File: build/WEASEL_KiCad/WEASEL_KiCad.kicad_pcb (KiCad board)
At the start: 2 copper layers, 355 x 80 mm, 56 parts

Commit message: Layout design
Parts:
- added REF**: Panel Jack, SimpleSynthPanel:Panel Jack, F.Cu at (314.0, 60.0)
- added REF**: Panel Jack, SimpleSynthPanel:Panel Jack, F.Cu at (244.0, 90.0)
- added REF**: Panel Jack, SimpleSynthPanel:Panel Jack, F.Cu at (269.0, 127.5)
- added REF**: Panel Jack, SimpleSynthPanel:Panel Jack, F.Cu at (244.0, 135.0)
- added REF**: Panel Jack, SimpleSynthPanel:Panel Jack, F.Cu at (304.0, 67.5)
- added REF**: Panel Jack, SimpleSynthPanel:Panel Jack, F.Cu at (314.0, 75.0)
- added REF**: Panel Jack, SimpleSynthPanel:Panel Jack, F.Cu at (279.0, 90.0)
- added REF**: Panel Jack, SimpleSynthPanel:Panel Jack, F.Cu at (244.0, 120.0)
- added REF**: Panel Jack, SimpleSynthPanel:Panel Jack, F.Cu at (259.0, 135.0)
- added REF**: Panel Jack, SimpleSynthPanel:Panel Jack, F.Cu at (304.0, 97.5)
- added REF**: Panel Jack, SimpleSynthPanel:Panel Jack, F.Cu at (314.0, 120.0)
- added REF**: Panel Jack, SimpleSynthPanel:Panel Jack, F.Cu at (259.0, 120.0)
- added REF**: Panel Jack, SimpleSynthPanel:Panel Jack, F.Cu at (314.0, 105.0)
- added REF**: Panel Jack, SimpleSynthPanel:Panel Jack, F.Cu at (244.0, 105.0)
- added REF**: Panel Jack, SimpleSynthPanel:Panel Jack, F.Cu at (224.0, 135.0)
- added REF**: Panel Jack, SimpleSynthPanel:Panel Jack, F.Cu at (294.0, 135.0)
- added REF**: Panel Jack, SimpleSynthPanel:Panel Jack, F.Cu at (304.0, 127.5)
- added REF**: Panel Jack, SimpleSynthPanel:Panel Jack, F.Cu at (279.0, 105.0)
- added REF**: Panel Jack, SimpleSynthPanel:Panel Jack, F.Cu at (314.0, 135.0)
- added REF**: ToggleSwitch_MTS-202_DPDT, DIYSynthMNL:PanelHole_ToggleSwitch_MTS-202, F.Cu at (105.0, 124.5)
- added REF**: Panel Jack, SimpleSynthPanel:Panel Jack, F.Cu at (193.5, 127.5)
- added REF**: Panel Jack, SimpleSynthPanel:Panel Jack, F.Cu at (294.0, 105.0)
- added REF**: Panel Jack, SimpleSynthPanel:Panel Jack, F.Cu at (259.0, 105.0)
- added REF**: Panel Jack, SimpleSynthPanel:Panel Jack, F.Cu at (224.0, 120.0)
- added REF**: Panel Jack, SimpleSynthPanel:Panel Jack, F.Cu at (259.0, 75.0)
- added REF**: Panel Jack, SimpleSynthPanel:Panel Jack, F.Cu at (279.0, 60.0)
- added REF**: Panel Jack, SimpleSynthPanel:Panel Jack, F.Cu at (224.0, 90.0)
- added REF**: Panel Jack, SimpleSynthPanel:Panel Jack, F.Cu at (224.0, 105.0)
- added REF**: Panel Jack, SimpleSynthPanel:Panel Jack, F.Cu at (234.0, 127.5)
- added REF**: Panel Jack, SimpleSynthPanel:Panel Jack, F.Cu at (259.0, 90.0)
- added REF**: Panel Jack, SimpleSynthPanel:Panel Jack, F.Cu at (279.0, 75.0)
- added REF**: ToggleSwitch_MTS-202_DPDT, DIYSynthMNL:PanelHole_ToggleSwitch_MTS-202, F.Cu at (198.5, 103.5)
- added REF**: Panel Jack, SimpleSynthPanel:Panel Jack, F.Cu at (279.0, 120.0)
- added REF**: Panel Jack, SimpleSynthPanel:Panel Jack, F.Cu at (294.0, 75.0)
- added REF**: Panel Jack, SimpleSynthPanel:Panel Jack, F.Cu at (234.0, 97.5)
- added REF**: Panel Jack, SimpleSynthPanel:Panel Jack, F.Cu at (203.5, 120.0)
- added REF**: Panel Jack, SimpleSynthPanel:Panel Jack, F.Cu at (203.5, 135.0)
- added REF**: Panel Jack, SimpleSynthPanel:Panel Jack, F.Cu at (314.0, 90.0)
- added REF**: Panel Jack, SimpleSynthPanel:Panel Jack, F.Cu at (269.0, 67.5)
- added REF**: Panel Jack, SimpleSynthPanel:Panel Jack, F.Cu at (269.0, 97.5)
- added REF**: ToggleSwitch_MTS-202_DPDT, DIYSynthMNL:PanelHole_ToggleSwitch_MTS-202, F.Cu at (105.0, 109.5)
- added REF**: Panel Jack, SimpleSynthPanel:Panel Jack, F.Cu at (279.0, 135.0)
- added REF**: Panel Jack, SimpleSynthPanel:Panel Jack, F.Cu at (259.0, 60.0)
- moved ? 377.0 mm to (-12.0, 90.0)
- moved ? 377.0 mm to (-12.0, 160.0)
- moved REF** 208.8 mm to (224.0, 75.0)
- moved REF** 208.8 mm to (224.0, 60.0)
- moved REF** 204.9 mm to (234.0, 67.5)
- moved REF** 201.1 mm to (244.0, 60.0)
- moved REF** 201.1 mm to (244.0, 75.0)
- moved REF** 165.2 mm to (117.5, 65.0)
- moved REF** 159.1 mm to (204.0, 80.0) (x2)
- moved REF** 159.1 mm to (166.5, 65.0)
- moved REF** 159.1 mm to (189.0, 80.0) (x2)
- moved REF** 159.1 mm to (159.0, 80.0)
- moved REF** 159.1 mm to (174.0, 80.0)
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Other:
- board size 355 x 80 mm -> 313 x 99 mm
- board text added: "- +"
- board text added: "Attack"
- board text added: "COMPLEX OSCILLATOR"
- board text added: "Complex Osc. Pitch"
- board text added: "Complex Osc. Timbre"
- board text added: "ENVELOPE"
- board text added: "Envelope Generator"
- board text added: "Fine Tune"
- board text added: "Frequency"
- board text added: "LOW-PASS GATE/VCA"
- board text added: "Level 1"
- board text added: "Level 2"
- board text added: "MODULATION OSCILLATOR"
- board text added: "Mod Osc. Frequency"
- board text added: "Mod Osc. Modulation"
- board text added: "Modulation"
- board text added: "PULSER"
- board text added: "PWM"
- board text added: "Pitch"
- board text added: "Pulser"
- board text added: "RANDOM VOLTAGE"
- board text added: "Random Voltage"
- board text added: "Release"
- board text added: "SEQUENCER"
- board text added: "Sequencer"
- board text added: "Sustain"
- board text added: "Timbre"

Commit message: Virtual Patch bay added to schematic
Virtual modular patch bay added
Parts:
- moved REF** 374.4 mm to (-60.0, 77.0)
- moved REF** 374.4 mm to (-130.0, 107.0)
- moved REF** 374.4 mm to (-105.0, 144.5)
- moved REF** 374.4 mm to (-130.0, 152.0)
- moved REF** 374.4 mm to (-70.0, 84.5)
- moved REF** 374.4 mm to (-170.0, 97.0)
- moved REF** 374.4 mm to (-150.0, 92.0)
- moved REF** 374.4 mm to (-299.0, 134.0)
- moved REF** 374.4 mm to (-329.0, 119.0)
- moved REF** 374.4 mm to (-130.0, 77.0)
- moved REF** 374.4 mm to (-60.0, 92.0)
- moved REF** 374.4 mm to (-329.0, 149.0)
- moved REF** 374.4 mm to (-279.0, 82.0)
- moved REF** 374.4 mm to (-329.0, 134.0)
- moved REF** 374.4 mm to (-256.5, 82.0)
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
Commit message: Schematic and PCB Changes
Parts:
- removed ? (x3): , 
- removed REF** (x45): Panel Jack, SimpleSynthPanel:Panel Jack
- removed REF** (x27): Panel Knob 1P, SimpleSynthPanel:Panel Knob 1P
- removed REF** (x15): ToggleSwitch_MTS-202_DPDT, DIYSynthMNL:PanelHole_ToggleSwitch_MTS-202
- removed REF** (x7): LED_HOLE, DIYSynthMNL:LED_HOLE
- removed REF**: MountingHole_M3_Standoff, DIYSynthMNL:MountingHole_M3_Standoff
- added C1: 10nF, DIYSynthMNL:C_Rect_L7.0mm_W2.0mm_P5.00mm_BigPads, F.Cu at (-3.00, 100.5)
- added C10: 10nF, DIYSynthMNL:C_Rect_L7.0mm_W2.0mm_P5.00mm_BigPads, F.Cu at (5.55, 100.5)
- added C11: 10nF, DIYSynthMNL:C_Rect_L7.0mm_W2.0mm_P5.00mm_BigPads, F.Cu at (5.55, 104.0)
- added C12: 10nF, DIYSynthMNL:C_Rect_L7.0mm_W2.0mm_P5.00mm_BigPads, F.Cu at (5.55, 107.6)
- added C13: 10nF, DIYSynthMNL:C_Rect_L7.0mm_W2.0mm_P5.00mm_BigPads, F.Cu at (5.55, 111.2)
- added C14: 10nF, DIYSynthMNL:C_Rect_L7.0mm_W2.0mm_P5.00mm_BigPads, F.Cu at (5.55, 114.7)
- added C15: 10nF, DIYSynthMNL:C_Rect_L7.0mm_W2.0mm_P5.00mm_BigPads, F.Cu at (5.55, 118.2)
- added C16: 10nF, DIYSynthMNL:C_Rect_L7.0mm_W2.0mm_P5.00mm_BigPads, F.Cu at (5.55, 121.8)
- added C17: 10nF, DIYSynthMNL:C_Rect_L7.0mm_W2.0mm_P5.00mm_BigPads, F.Cu at (-250.6, 162.7)
- added C18: 10nF, DIYSynthMNL:C_Rect_L7.0mm_W2.0mm_P5.00mm_BigPads, F.Cu at (-250.6, 166.2)
- added C19: 10nF, DIYSynthMNL:C_Rect_L7.0mm_W2.0mm_P5.00mm_BigPads, F.Cu at (-242.0, 137.8)
- added C2: 10nF, DIYSynthMNL:C_Rect_L7.0mm_W2.0mm_P5.00mm_BigPads, F.Cu at (-3.00, 104.0)
- added C20: 10nF, DIYSynthMNL:C_Rect_L7.0mm_W2.0mm_P5.00mm_BigPads, F.Cu at (-242.0, 141.4)
- added C21: 10nF, DIYSynthMNL:C_Rect_L7.0mm_W2.0mm_P5.00mm_BigPads, F.Cu at (-242.0, 144.9)
- added C22: 10nF, DIYSynthMNL:C_Rect_L7.0mm_W2.0mm_P5.00mm_BigPads, F.Cu at (-242.0, 148.5)
- added C23: 10nF, DIYSynthMNL:C_Rect_L7.0mm_W2.0mm_P5.00mm_BigPads, F.Cu at (-242.0, 152.0)
- added C24: 10nF, DIYSynthMNL:C_Rect_L7.0mm_W2.0mm_P5.00mm_BigPads, F.Cu at (-242.0, 155.6)
- added C25: 10nF, DIYSynthMNL:C_Rect_L7.0mm_W2.0mm_P5.00mm_BigPads, F.Cu at (-242.0, 159.1)
- added C26: 10nF, DIYSynthMNL:C_Rect_L7.0mm_W2.0mm_P5.00mm_BigPads, F.Cu at (-242.0, 162.7)
- added C3: 10nF, DIYSynthMNL:C_Rect_L7.0mm_W2.0mm_P5.00mm_BigPads, F.Cu at (-3.00, 107.6)
- added C4: 10nF, DIYSynthMNL:C_Rect_L7.0mm_W2.0mm_P5.00mm_BigPads, F.Cu at (-3.00, 111.2)
- added C5: 10nF, DIYSynthMNL:C_Rect_L7.0mm_W2.0mm_P5.00mm_BigPads, F.Cu at (-3.00, 114.7)
- added C6: 10nF, DIYSynthMNL:C_Rect_L7.0mm_W2.0mm_P5.00mm_BigPads, F.Cu at (-3.00, 118.2)
- added C7: 10nF, DIYSynthMNL:C_Rect_L7.0mm_W2.0mm_P5.00mm_BigPads, F.Cu at (-3.00, 121.8)
- added C8: 10nF, DIYSynthMNL:C_Rect_L7.0mm_W2.0mm_P5.00mm_BigPads, F.Cu at (-3.00, 125.3)
- added C9: 10nF, DIYSynthMNL:C_Rect_L7.0mm_W2.0mm_P5.00mm_BigPads, F.Cu at (-3.00, 128.9)
- added D1: 1N4148, DIYSynthMNL:D_4148_BigPads, F.Cu at (-259.0, 76.8)
- added D2: 1N4148, DIYSynthMNL:D_4148_BigPads, F.Cu at (-259.0, 80.4)
- added D3: 1N4148, DIYSynthMNL:D_4148_BigPads, F.Cu at (-259.0, 83.9)
- added D30: 1N4148, DIYSynthMNL:D_4148_BigPads, F.Cu at (-247.5, 76.8)
- added D31: 1N4148, DIYSynthMNL:D_4148_BigPads, F.Cu at (-247.5, 80.4)
- added D32: 1N4148, DIYSynthMNL:D_4148_BigPads, F.Cu at (-247.5, 83.9)
- added D33: 1N4148, DIYSynthMNL:D_4148_BigPads, F.Cu at (-247.5, 87.5)
- added D34: 1N4148, DIYSynthMNL:D_4148_BigPads, F.Cu at (-247.5, 91.0)
- added D35: 1N4148, DIYSynthMNL:D_4148_BigPads, F.Cu at (-247.5, 94.6)
- added D36: 1N4148, DIYSynthMNL:D_4148_BigPads, F.Cu at (-247.5, 98.1)
- added D37: 1N4148, DIYSynthMNL:D_4148_BigPads, F.Cu at (-247.5, 101.7)
- added D38: 1N4148, DIYSynthMNL:D_4148_BigPads, F.Cu at (-236.1, 76.8)
- added D39: 1N4148, DIYSynthMNL:D_4148_BigPads, F.Cu at (-236.1, 80.4)
- added D4: 1N4148, DIYSynthMNL:D_4148_BigPads, F.Cu at (-259.0, 87.5)
- added D40: 1N4148, DIYSynthMNL:D_4148_BigPads, F.Cu at (-236.1, 83.9)
- added D41: 1N4148, DIYSynthMNL:D_4148_BigPads, F.Cu at (-236.1, 87.5)
- added D42: 1N4148, DIYSynthMNL:D_4148_BigPads, F.Cu at (-236.1, 91.0)
- added D43: 1N4148, DIYSynthMNL:D_4148_BigPads, F.Cu at (-236.1, 94.6)
- added D44: 1N4148, DIYSynthMNL:D_4148_BigPads, F.Cu at (297.6, 43.5)
- added D45: 1N4148, DIYSynthMNL:D_4148_BigPads, F.Cu at (-213.0, 109.3)
- added D46: 1N4148, DIYSynthMNL:D_4148_BigPads, F.Cu at (-213.0, 112.8)
- added D47: 1N4148, DIYSynthMNL:D_4148_BigPads, F.Cu at (-213.0, 116.4)
- added D48: 1N4148, DIYSynthMNL:D_4148_BigPads, F.Cu at (-213.0, 120.0)
- added D49: 1N4148, DIYSynthMNL:D_4148_BigPads, F.Cu at (-213.0, 123.5)
- added D5: 1N4148, DIYSynthMNL:D_4148_BigPads, F.Cu at (-259.0, 91.0)
- added D6: 1N4148, DIYSynthMNL:D_4148_BigPads, F.Cu at (-259.0, 94.6)
- added D7: 1N4148, DIYSynthMNL:D_4148_BigPads, F.Cu at (-259.0, 98.1)
- added D8: 1N4148, DIYSynthMNL:D_4148_BigPads, F.Cu at (-259.0, 101.7)
- added J1: MIDI IN, Connector_Audio:Jack_3.5mm_CUI_SJ1-3523N_Horizontal, F.Cu at (294.3, 30.0)
- added J10: LPG_LEVEL2CTRL, Connector_Audio:Jack_3.5mm_QingPu_WQP-PJ398SM_Vertical_CircularHoles, F.Cu at (215.0, 161.7)
- added J14: SEQ_OUTPUT2, Connector_Audio:Jack_3.5mm_QingPu_WQP-PJ398SM_Vertical_CircularHoles, F.Cu at (125.0, 151.7)
- added J15: SEQ_OUTPUT3, Connector_Audio:Jack_3.5mm_QingPu_WQP-PJ398SM_Vertical_CircularHoles, F.Cu at (185.0, 151.7)
- added J16: EG_OUTPUT1, Connector_Audio:Jack_3.5mm_QingPu_WQP-PJ398SM_Vertical_CircularHoles, F.Cu at (110.0, 151.7)
- added J17: EG_OUTPUT2, Connector_Audio:Jack_3.5mm_QingPu_WQP-PJ398SM_Vertical_CircularHoles, F.Cu at (170.0, 151.7)
- added J18: EG_OUTPUT3, Connector_Audio:Jack_3.5mm_QingPu_WQP-PJ398SM_Vertical_CircularHoles, F.Cu at (230.0, 151.7)
- added J19: PLSR_OUTPUT1, Connector_Audio:Jack_3.5mm_QingPu_WQP-PJ398SM_Vertical_CircularHoles, F.Cu at (50.0, 171.7)
- added J2: STEREO_OUTPUT, Connector_Audio:Jack_3.5mm_CUI_SJ1-3523N_Horizontal, F.Cu at (275.5, 30.0)
- added J20: PLSR_OUTPUT2, Connector_Audio:Jack_3.5mm_QingPu_WQP-PJ398SM_Vertical_CircularHoles, F.Cu at (125.0, 171.7)
- added J21: PLSR_OUTPUT3, Connector_Audio:Jack_3.5mm_QingPu_WQP-PJ398SM_Vertical_CircularHoles, F.Cu at (185.0, 171.7)
- added J22: RNDM_OUTPUT1, Connector_Audio:Jack_3.5mm_QingPu_WQP-PJ398SM_Vertical_CircularHoles, F.Cu at (110.0, 171.7)
- added J23: RNDM_OUTPUT2, Connector_Audio:Jack_3.5mm_QingPu_WQP-PJ398SM_Vertical_CircularHoles, F.Cu at (170.0, 171.7)
- added J24: RNDM_OUTPUT3, Connector_Audio:Jack_3.5mm_QingPu_WQP-PJ398SM_Vertical_CircularHoles, F.Cu at (230.0, 171.7)
- added J3: SEQ_OUTPUT1, Connector_Audio:Jack_3.5mm_QingPu_WQP-PJ398SM_Vertical_CircularHoles, F.Cu at (50.0, 151.7)
- added J4: PLSR_PERIODCTRL, Connector_Audio:Jack_3.5mm_QingPu_WQP-PJ398SM_Vertical_CircularHoles, F.Cu at (65.0, 161.7)
- added J5: MODOSC_FREQCTRL, Connector_Audio:Jack_3.5mm_QingPu_WQP-PJ398SM_Vertical_CircularHoles, F.Cu at (80.0, 161.7)
- added J6: MODOSC_MODCTRL, Connector_Audio:Jack_3.5mm_QingPu_WQP-PJ398SM_Vertical_CircularHoles, F.Cu at (95.0, 161.7)
- added J7: COMPOSC_PITCHCTRL, Connector_Audio:Jack_3.5mm_QingPu_WQP-PJ398SM_Vertical_CircularHoles, F.Cu at (140.0, 161.7)
- added J8: COMPOSC_WAVEFOLDERCTRL, Connector_Audio:Jack_3.5mm_QingPu_WQP-PJ398SM_Vertical_CircularHoles, F.Cu at (155.0, 161.7)
- added J9: LPG_LEVEL1CTRL, Connector_Audio:Jack_3.5mm_QingPu_WQP-PJ398SM_Vertical_CircularHoles, F.Cu at (200.0, 161.7)
- added R1: 10k, PCM_4ms_Resistor:R_Axial_DIN0207_L6.3mm_D2.5mm_P7.62mm_Horizontal, F.Cu at (307.0, 57.0)
- added R10: 220R, PCM_4ms_Resistor:R_Axial_DIN0207_L6.3mm_D2.5mm_P7.62mm_Horizontal, F.Cu at (295.4, 39.5)
- added R2: 10k, PCM_4ms_Resistor:R_Axial_DIN0207_L6.3mm_D2.5mm_P7.62mm_Horizontal, F.Cu at (307.0, 59.5)
- added R3: 10k, PCM_4ms_Resistor:R_Axial_DIN0207_L6.3mm_D2.5mm_P7.62mm_Horizontal, F.Cu at (336.3, 67.0)
- added R4: 10k, PCM_4ms_Resistor:R_Axial_DIN0207_L6.3mm_D2.5mm_P7.62mm_Horizontal, F.Cu at (336.3, 64.5)
- added R5: 10k, PCM_4ms_Resistor:R_Axial_DIN0207_L6.3mm_D2.5mm_P7.62mm_Horizontal, F.Cu at (336.3, 62.0)
- added R6: 10k, PCM_4ms_Resistor:R_Axial_DIN0207_L6.3mm_D2.5mm_P7.62mm_Horizontal, F.Cu at (336.3, 59.5)
- added R7: 10k, PCM_4ms_Resistor:R_Axial_DIN0207_L6.3mm_D2.5mm_P7.62mm_Horizontal, F.Cu at (336.3, 57.0)
- added R8: 10k, PCM_4ms_Resistor:R_Axial_DIN0207_L6.3mm_D2.5mm_P7.62mm_Horizontal, F.Cu at (336.3, 54.5)
- added R9: 220R, PCM_4ms_Resistor:R_Axial_DIN0207_L6.3mm_D2.5mm_P7.62mm_Horizontal, F.Cu at (293.8, 59.0)
- added RV1: SQ_Step1, DIYSynthMNL:Potentiometer_RV09_BigPads, F.Cu at (47.5, 80.0)
- added RV10: PLSR_PERIOD, DIYSynthMNL:Potentiometer_RV09_BigPads, F.Cu at (137.5, 120.0)
- added RV11: MODOSC_FREQCTRL, DIYSynthMNL:Potentiometer_RV09_BigPads, F.Cu at (168.0, 120.0)
- added RV12: MODOSC_FREQ, DIYSynthMNL:Potentiometer_RV09_BigPads, F.Cu at (188.0, 120.0)
- added RV13: MODOSC_MODULATIONCTRL, DIYSynthMNL:Potentiometer_RV09_BigPads, F.Cu at (208.0, 120.0)
- added RV14: MODOSC_MODULATION, DIYSynthMNL:Potentiometer_RV09_BigPads, F.Cu at (228.0, 120.0)
- added RV15: MODOSC_FINE, DIYSynthMNL:Potentiometer_RV09_BigPads, F.Cu at (168.0, 100.0)
- added RV16: COMPLEXOSC_FREQCTRL, DIYSynthMNL:Potentiometer_RV09_BigPads, F.Cu at (168.0, 80.0)
- added RV17: COMPLEXOSC_FREQ, DIYSynthMNL:Potentiometer_RV09_BigPads, F.Cu at (188.0, 80.0)
- added RV18: COMPLEXOSC_FINE, DIYSynthMNL:Potentiometer_RV09_BigPads, F.Cu at (188.0, 60.0)
- added RV19: COMPLEXOSC_WAVEFOLDERCTRL, DIYSynthMNL:Potentiometer_RV09_BigPads, F.Cu at (208.0, 80.0)
- added RV2: SQ_Step2, DIYSynthMNL:Potentiometer_RV09_BigPads, F.Cu at (67.5, 80.0)
- added RV20: COMPLEXOSC_WAVEFOLDER, DIYSynthMNL:Potentiometer_RV09_BigPads, F.Cu at (228.0, 80.0)
- added RV21: COMPLEXOSC_TIMBRE, DIYSynthMNL:Potentiometer_RV09_BigPads, F.Cu at (228.0, 60.0)
- added RV22: LPG_LEVEL1CTRL, DIYSynthMNL:Potentiometer_RV09_BigPads, F.Cu at (258.0, 80.0)
- added RV23: LPG_LEVEL1, DIYSynthMNL:Potentiometer_RV09_BigPads, F.Cu at (278.0, 80.0)
- added RV24: LPG_LEVEL2CTRL, DIYSynthMNL:Potentiometer_RV09_BigPads, F.Cu at (258.0, 120.0)
- added RV25: LPG_LEVEL2, DIYSynthMNL:Potentiometer_RV09_BigPads, F.Cu at (278.0, 120.0)
- added RV26: CLOCK, DIYSynthMNL:Potentiometer_RV09_BigPads, F.Cu at (308.0, 120.0)
- added RV3: SQ_Step3, DIYSynthMNL:Potentiometer_RV09_BigPads, F.Cu at (87.5, 80.0)
- added RV4: SQ_Step4, DIYSynthMNL:Potentiometer_RV09_BigPads, F.Cu at (107.5, 80.0)
- added RV5: SQ_Step5, DIYSynthMNL:Potentiometer_RV09_BigPads, F.Cu at (128.0, 80.0)
- added RV6: EG_ATTACK, DIYSynthMNL:Potentiometer_RV09_BigPads, F.Cu at (47.5, 120.0)
- added RV7: EG_SUSTAIN, DIYSynthMNL:Potentiometer_RV09_BigPads, F.Cu at (87.5, 120.0)
- added RV8: EG_DECAY, DIYSynthMNL:Potentiometer_RV09_BigPads, F.Cu at (67.5, 120.0)
- added RV9: PLSR_PERIODCTRL, DIYSynthMNL:Potentiometer_RV09_BigPads, F.Cu at (117.5, 120.0)
- added SW1: SQ_TOGGLESTEP1, DIYSynthMNL:ToggleSwitch_MTS-102_SPDT, F.Cu at (45.0, 67.5)
- added SW2: SEQ_TRIGGERSELECT, PCM_4ms_Experimental_FP:SW_PUSH_6mm_H13mm, F.Cu at (45.0, 47.5)
- added SW3: SQ_TOGGLESTEP2, DIYSynthMNL:ToggleSwitch_MTS-102_SPDT, F.Cu at (65.0, 67.5)
- added SW31: EG_TRIGGERSELECT, PCM_4ms_Experimental_FP:SW_PUSH_6mm_H13mm, F.Cu at (45.0, 107.5)
- added SW32: EG_MODESELECT, PCM_4ms_Experimental_FP:SW_PUSH_6mm_H13mm, F.Cu at (65.0, 107.5)
- added SW33: PLSR_TRIGGERSELECT, PCM_4ms_Experimental_FP:SW_PUSH_6mm_H13mm, F.Cu at (115.0, 107.5)
- added SW34: PLSR_MODE, PCM_4ms_Experimental_FP:SW_PUSH_6mm_H13mm, F.Cu at (135.0, 107.5)
- added SW35: MODOSC_MIDITOGGLE, PCM_4ms_Experimental_FP:SW_PUSH_6mm_H13mm, F.Cu at (205.5, 107.5)
- added SW36: MODOSC_PITCHTRANGE, PCM_4ms_Experimental_FP:SW_PUSH_6mm_H13mm, F.Cu at (185.5, 107.5)
- added SW37: COMPLEXOSC_MIDITOGGLE, PCM_4ms_Experimental_FP:SW_PUSH_6mm_H13mm, F.Cu at (225.5, 107.5)
- added SW38: COMPLEXOSC_POLARITY, PCM_4ms_Experimental_FP:SW_PUSH_6mm_H13mm, F.Cu at (165.5, 67.5)
- added SW39: COMPLEXOSC_WAVETOGGLE, PCM_4ms_Experimental_FP:SW_PUSH_6mm_H13mm, F.Cu at (205.5, 67.5)
- added SW4: SQ_TOGGLESTEP3, DIYSynthMNL:ToggleSwitch_MTS-102_SPDT, F.Cu at (85.0, 67.5)
- added SW40: LPG_GATE1MODE, PCM_4ms_Experimental_FP:SW_PUSH_6mm_H13mm, F.Cu at (255.5, 107.5)
- added SW41: LPG_GATE2MODE, PCM_4ms_Experimental_FP:SW_PUSH_6mm_H13mm, F.Cu at (275.5, 107.5)
- added SW42: RNDMVOLTAGE_TRIGGERSELECT, PCM_4ms_Experimental_FP:SW_PUSH_6mm_H13mm, F.Cu at (125.5, 47.5)
- added SW43: CLOCK_SYNCTOGGLE, PCM_4ms_Experimental_FP:SW_PUSH_6mm_H13mm, F.Cu at (305.5, 107.5)
- added SW5: SQ_TOGGLESTEP4, DIYSynthMNL:ToggleSwitch_MTS-102_SPDT, F.Cu at (105.0, 67.5)
- added SW6: SEQ_STAGES, PCM_4ms_Experimental_FP:SW_PUSH_6mm_H13mm, F.Cu at (65.0, 47.5)
- added SW7: SQ_TOGGLESTEP5, DIYSynthMNL:ToggleSwitch_MTS-102_SPDT, F.Cu at (125.5, 67.5)
- added U1: CD74HC4067M, Package_SO:SOIC-24W_7.5x15.4mm_P1.27mm, F.Cu at (-254.5, 127.6)
- added U2: CD74HC4067M, Package_SO:SOIC-24W_7.5x15.4mm_P1.27mm, F.Cu at (-241.6, 127.6)
- added U3: 6N138, DIYSynthMNL:DIP-8_W7.62mm_LongPads, F.Cu at (297.4, 48.0)
- moved A1 279.3 mm to (314.3, 26.5)
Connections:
- A1 pad 1: unconnected-(A1-USB_ID-Pad1) -> MUX1_S0
- A1 pad 10: unconnected-(A1-SPI1_POCI-Pad10) -> Y1
- A1 pad 11: unconnected-(A1-SPI1_PICO-Pad11) -> Y2
- A1 pad 12: unconnected-(A1-I2C1_SCL-Pad12) -> Y3
- A1 pad 13: unconnected-(A1-I2C1_SDA-Pad13) -> X0
- A1 pad 14: unconnected-(A1-USART1_TX-Pad14) -> X1
- A1 pad 15: unconnected-(A1-USART1_RX-Pad15) -> Y4
- A1 pad 18: unconnected-(A1-AUDIO_OUT_1-Pad18) -> OUT_L
- A1 pad 19: unconnected-(A1-AUDIO_OUT_2-Pad19) -> OUT_R
- A1 pad 2: unconnected-(A1-SD_DATA_3-Pad2) -> MUX1_S1
- A1 pad 20: unconnected-(A1-AGND-Pad20) -> GND
- A1 pad 22: unconnected-(A1-ADC_0-Pad22) -> MUX1_SIGNAL
- A1 pad 23: unconnected-(A1-ADC_1-Pad23) -> MUX2_SIGNAL
- A1 pad 24: unconnected-(A1-ADC_2-Pad24) -> X2
- A1 pad 25: unconnected-(A1-ADC_3-Pad25) -> X3
- A1 pad 26: unconnected-(A1-ADC_4-Pad26) -> B0
- A1 pad 27: unconnected-(A1-ADC_5-Pad27) -> B1
- A1 pad 28: unconnected-(A1-ADC_6-Pad28) -> B2
- A1 pad 29: unconnected-(A1-DAC_OUT2-Pad29) -> B3
- A1 pad 3: unconnected-(A1-SD_DATA_2-Pad3) -> MUX1_S2
- A1 pad 30: unconnected-(A1-DAC_OUT1-Pad30) -> A0
- A1 pad 31: unconnected-(A1-SAI2_MCLK-Pad31) -> A1
- A1 pad 32: unconnected-(A1-SAI2_SD_B-Pad32) -> A2
- A1 pad 33: unconnected-(A1-SAI2_SD_A-Pad33) -> A3
- A1 pad 34: unconnected-(A1-SAI2_FS-Pad34) -> A4
- A1 pad 35: unconnected-(A1-SAI2_SCK-Pad35) -> A5
- A1 pad 36: unconnected-(A1-USB_D_--Pad36) -> A6
- A1 pad 37: unconnected-(A1-USB_D_+-Pad37) -> MIDI_INPUT
- A1 pad 38: unconnected-(A1-3V3_D-Pad38) -> Vcc
- A1 pad 4: unconnected-(A1-SD_DATA_1-Pad4) -> MUX1_S3
- A1 pad 40: unconnected-(A1-DGND-Pad40) -> GND
- A1 pad 5: unconnected-(A1-SD_DATA_0-Pad5) -> MUX2_S0
- A1 pad 6: unconnected-(A1-SD_CMD-Pad6) -> MUX2_S1
- A1 pad 7: unconnected-(A1-SD_CLK-Pad7) -> MUX2_S2
- A1 pad 8: unconnected-(A1-SPI1_CS-Pad8) -> MUX2_S3
- A1 pad 9: unconnected-(A1-SPI1_SCK-Pad9) -> Y0
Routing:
- net OUT_R: track 0.00 -> 131.4 mm
- net OUT_L: track 0.00 -> 110.0 mm
- net Net-(D44-A): track 0.00 -> 15.3 mm
- net Net-(D44-K): track 0.00 -> 12.7 mm
- net Net-(J1-PadR): track 0.00 -> 4.50 mm
- net MIDI_INPUT: track 0.00 -> 4.35 mm
- net Vcc: track 0.00 -> 3.46 mm
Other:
- board size 313 x 99 mm -> 325 x 180 mm
- board text added: "LINE OUT"
- board text added: "MIDI IN"
- board text removed: "- +"
- board text removed: "Attack"
- board text removed: "COMPLEX OSCILLATOR"
- board text removed: "Complex Osc. Pitch"
- board text removed: "Complex Osc. Timbre"
- board text removed: "ENVELOPE"
- board text removed: "Envelope Generator"
- board text removed: "Fine Tune"
- board text removed: "Frequency"
- board text removed: "LOW-PASS GATE/VCA"
- board text removed: "Level 1"
- board text removed: "Level 2"
- board text removed: "MODULATION OSCILLATOR"
- board text removed: "Mod Osc. Frequency"
- board text removed: "Mod Osc. Modulation"
- board text removed: "Modulation"
- board text removed: "PULSER"
- board text removed: "PWM"
- board text removed: "Pitch"
- board text removed: "Pulser"
- board text removed: "RANDOM VOLTAGE"
- board text removed: "Random Voltage"
- board text removed: "Release"
- board text removed: "SEQUENCER"
- board text removed: "Sequencer"
- board text removed: "Sustain"
- board text removed: "Timbre"

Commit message: pcb update
update based on schematic changes
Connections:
- D4 pad 1: unconnected-(D4-K-Pad1) -> A3
- D4 pad 2: unconnected-(D4-A-Pad2) -> Net-(D4-A)
- D8 pad 1: unconnected-(D8-K-Pad1) -> A6
- D8 pad 2: unconnected-(D8-A-Pad2) -> Net-(D8-A)
- J10 pad S: Net-(J10-PadS) -> Net-(D8-A)
- J10 pad T: Net-(J10-PadS) -> Net-(D8-A)
- J10 pad TN: Net-(J10-PadS) -> Net-(D8-A)
- J7 pad S: Net-(J7-PadS) -> Net-(D4-A)
- J7 pad T: Net-(J7-PadS) -> Net-(D4-A)
- J7 pad TN: Net-(J7-PadS) -> Net-(D4-A)
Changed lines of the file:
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@@
 	(net 94 "A5")
 	(net 95 "A6")
-	(net 96 "unconnected-(D4-K-Pad1)")
-	(net 97 "unconnected-(D4-A-Pad2)")
-	(net 98 "unconnected-(D8-A-Pad2)")
-	(net 99 "unconnected-(D8-K-Pad1)")
-	(net 100 "Net-(J7-PadS)")
-	(net 101 "Net-(J10-PadS)")
-	(net 102 "unconnected-(U2-I12-Pad19)")
-	(net 103 "unconnected-(U2-I10-Pad21)")
-	(net 104 "unconnected-(U2-I11-Pad20)")
-	(net 105 "Net-(D45-A)")
-	(net 106 "Net-(D46-A)")
-	(net 107 "Net-(D47-A)")
-	(net 108 "Net-(D48-A)")
-	(net 109 "Net-(D49-A)")
-	(net 110 "unconnected-(SW1-C-Pad3)")
-	(net 111 "unconnected-(SW3-C-Pad3)")
-	(net 112 "unconnected-(SW4-C-Pad3)")
-	(net 113 "unconnected-(SW5-C-Pad3)")
-	(net 114 "unconnected-(SW7-C-Pad3)")
+	(net 96 "Net-(D4-A)")
+	(net 97 "Net-(D8-A)")
+	(net 98 "unconnected-(U2-I12-Pad19)")
+	(net 99 "unconnected-(U2-I10-Pad21)")
+	(net 100 "unconnected-(U2-I11-Pad20)")
+	(net 101 "Net-(D45-A)")
+	(net 102 "Net-(D46-A)")
+	(net 103 "Net-(D47-A)")
+	(net 104 "Net-(D48-A)")
+	(net 105 "Net-(D49-A)")
+	(net 106 "unconnected-(SW1-C-Pad3)")
+	(net 107 "unconnected-(SW3-C-Pad3)")
+	(net 108 "unconnected-(SW4-C-Pad3)")
+	(net 109 "unconnected-(SW5-C-Pad3)")
+	(net 110 "unconnected-(SW7-C-Pad3)")
 	(footprint "PCM_4ms_Experimental_FP:SW_PUSH_6mm_H13mm"
 		(layer "F.Cu")
@@
 			(layers "*.Cu" "*.Mask")
 			(remove_unused_layers no)
-			(net 101 "Net-(J10-PadS)")
+			(net 97 "Net-(D8-A)")
 			(pintype "passive")
 		)
@@
 			(layers "*.Cu" "*.Mask")
 			(remove_unused_layers no)
-			(net 101 "Net-(J10-PadS)")
+			(net 97 "Net-(D8-A)")
 			(pintype "passive")
 		)
@@
 			(layers "*.Cu" "*.Mask")
 			(remove_unused_layers no)
-			(net 101 "Net-(J10-PadS)")
+			(net 97 "Net-(D8-A)")
 			(pintype "passive")
 		)
@@
 			(layers "*.Cu" "*.Mask")
 			(remove_unused_layers no)
-			(net 105 "Net-(D45-A)")
+			(net 101 "Net-(D45-A)")
 			(pinfunction "A")
 			(pintype "passive")
@@
 			(layers "*.Cu" "*.Mask")
 			(remove_unused_layers no)
-			(net 109 "Net-(D49-A)")
+			(net 105 "Net-(D49-A)")
 			(pinfunction "A")
 			(pintype "passive")
@@
 			(layers "*.Cu" "*.Mask")
 			(remove_unused_layers no)
-			(net 114 "unconnected-(SW7-C-Pad3)")
+			(net 110 "unconnected-(SW7-C-Pad3)")
 			(pinfunction "C")
 			(pintype "passive")
@@
 			(layers "*.Cu" "*.Mask")
 			(remove_unused_layers no)
-			(net 99 "unconnected-(D8-K-Pad1)")
+			(net 95 "A6")
 			(pinfunction "K")
 			(pintype "passive")
@@
 			(layers "*.Cu" "*.Mask")
 			(remove_unused_layers no)
-			(net 98 "unconnected-(D8-A-Pad2)")
+			(net 97 "Net-(D8-A)")
 			(pinfunction "A")
 			(pintype "passive")
@@
 			(layers "*.Cu" "*.Mask")
 			(remove_unused_layers no)
-			(net 109 "Net-(D49-A)")
+			(net 105 "Net-(D49-A)")
 			(pinfunction "A")
 			(pintype "passive")
@@
 			(layers "*.Cu" "*.Mask")
 			(remove_unused_layers no)
-			(net 105 "Net-(D45-A)")
+			(net 101 "Net-(D45-A)")
 			(pinfunction "A")
 			(pintype "passive")
@@
 			(layers "*.Cu" "*.Mask")
 			(remove_unused_layers no)
-			(net 110 "unconnected-(SW1-C-Pad3)")
+			(net 106 "unconnected-(SW1-C-Pad3)")
 			(pinfunction "C")
 			(pintype "passive")
@@
 			(layers "*.Cu" "*.Mask")
 			(remove_unused_layers no)
-			(net 106 "Net-(D46-A)")
+			(net 102 "Net-(D46-A)")
 			(pinfunction "A")
 			(pintype "passive")
@@
 			(layers "*.Cu" "*.Mask")
 			(remove_unused_layers no)
-			(net 107 "Net-(D47-A)")
+			(net 103 "Net-(D47-A)")
 			(pinfunction "A")
 			(pintype "passive")
@@
 			(layers "F.Cu" "F.Mask" "F.Paste")
 			(roundrect_rratio 0.25)
-			(net 102 "unconnected-(U2-I12-Pad19)")
+			(net 98 "unconnected-(U2-I12-Pad19)")
 			(pinfunction "I12")
 			(pintype "passive")
@@
 			(layers "F.Cu" "F.Mask" "F.Paste")
 			(roundrect_rratio 0.25)
-			(net 104 "unconnected-(U2-I11-Pad20)")
+			(net 100 "unconnected-(U2-I11-Pad20)")
 			(pinfunction "I11")
 			(pintype "passive")
@@
 			(layers "F.Cu" "F.Mask" "F.Paste")
 			(roundrect_rratio 0.25)
-			(net 103 "unconnected-(U2-I10-Pad21)")
+			(net 99 "unconnected-(U2-I10-Pad21)")
 			(pinfunction "I10")
 			(pintype "passive")
@@
 			(layers "*.Cu" "*.Mask")
 			(remove_unused_layers no)
-			(net 106 "Net-(D46-A)")
+			(net 102 "Net-(D46-A)")
 			(pinfunction "A")
 			(pintype "passive")
@@
 			(layers "*.Cu" "*.Mask")
 			(remove_unused_layers no)
-			(net 111 "unconnected-(SW3-C-Pad3)")
+			(net 107 "unconnected-(SW3-C-Pad3)")
 			(pinfunction "C")
 			(pintype "passive")
@@
 			(layers "*.Cu" "*.Mask")
 			(remove_unused_layers no)
-			(net 100 "Net-(J7-PadS)")
+			(net 96 "Net-(D4-A)")
 			(pintype "passive")
 		)
@@
 			(layers "*.Cu" "*.Mask")
 			(remove_unused_layers no)
-			(net 100 "Net-(J7-PadS)")
+			(net 96 "Net-(D4-A)")
 			(pintype "passive")
 		)
@@
 			(layers "*.Cu" "*.Mask")
 			(remove_unused_layers no)
-			(net 100 "Net-(J7-PadS)")
+			(net 96 "Net-(D4-A)")
 			(pintype "passive")
 		)
@@
 			(layers "*.Cu" "*.Mask")
 			(remove_unused_layers no)
-			(net 108 "Net-(D48-A)")
+			(net 104 "Net-(D48-A)")
 			(pinfunction "A")
 			(pintype "passive")
@@
 			(layers "*.Cu" "*.Mask")
 			(remove_unused_layers no)
-			(net 96 "unconnected-(D4-K-Pad1)")
+			(net 88 "A3")
 			(pinfunction "K")
 			(pintype "passive")
@@
 			(layers "*.Cu" "*.Mask")
 			(remove_unused_layers no)
-			(net 97 "unconnected-(D4-A-Pad2)")
+			(net 96 "Net-(D4-A)")
 			(pinfunction "A")
 			(pintype "passive")
@@
 			(layers "*.Cu" "*.Mask")
 			(remove_unused_layers no)
-			(net 108 "Net-(D48-A)")
+			(net 104 "Net-(D48-A)")
 			(pinfunction "A")
 			(pintype "passive")
@@
 			(layers "*.Cu" "*.Mask")
 			(remove_unused_layers no)
-			(net 113 "unconnected-(SW5-C-Pad3)")
+			(net 109 "unconnected-(SW5-C-Pad3)")
 			(pinfunction "C")
 			(pintype "passive")
@@
 			(layers "*.Cu" "*.Mask")
 			(remove_unused_layers no)
-			(net 107 "Net-(D47-A)")
+			(net 103 "Net-(D47-A)")
 			(pinfunction "A")
 			(pintype "passive")
@@
 			(layers "*.Cu" "*.Mask")
 			(remove_unused_layers no)
-			(net 112 "unconnected-(SW4-C-Pad3)")
+			(net 108 "unconnected-(SW4-C-Pad3)")
 			(pinfunction "C")
 			(pintype "passive")

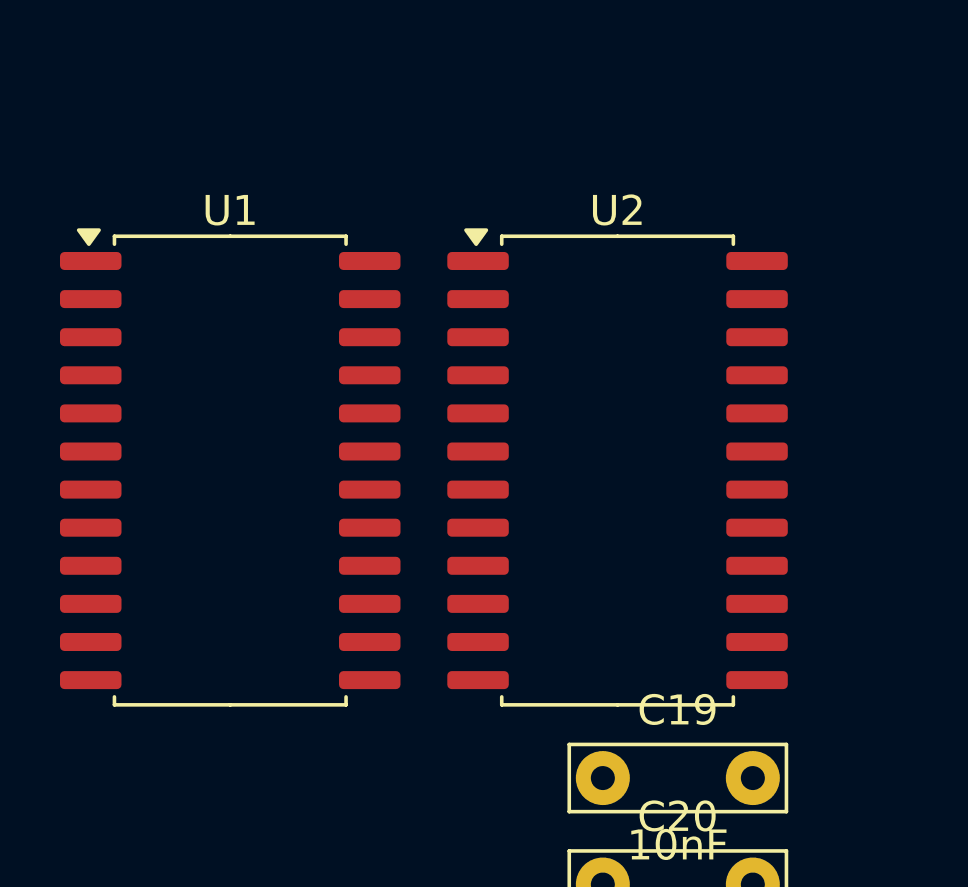
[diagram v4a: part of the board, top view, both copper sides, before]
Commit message: Update Schematic
- changed MUX to module instead of SMD IC
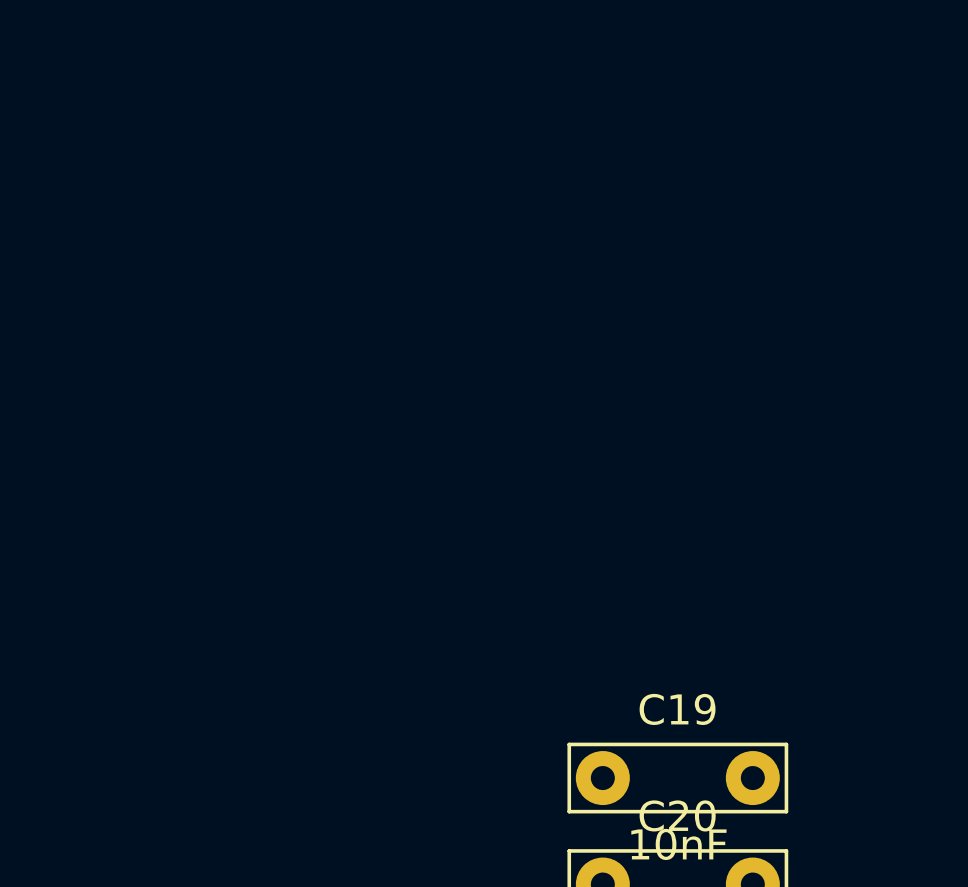
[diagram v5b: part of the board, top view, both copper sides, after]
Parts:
- removed U1, U2: CD74HC4067M, Package_SO:SOIC-24W_7.5x15.4mm_P1.27mm
